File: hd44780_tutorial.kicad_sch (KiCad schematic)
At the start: 28 parts, among them J1 LCD_2004_PinSocket_1x16_P2.54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, J2 USB4105-GF-A, SW1 REG SELECT, SW2 ENABLE, SW3 DS02C-254-1L-08BE

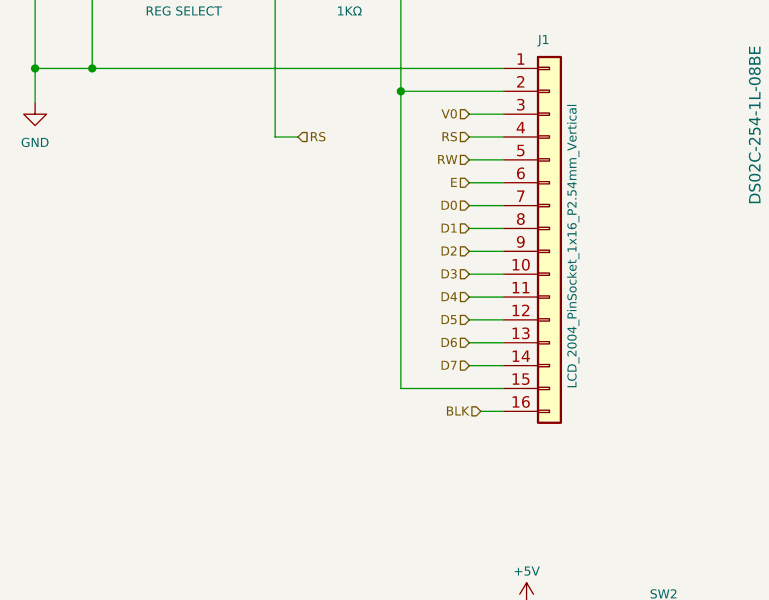
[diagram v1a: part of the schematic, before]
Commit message: Adjusted some copper tracks. Made all resistors horizontal. Added 1K network resistor for LCD data lines. Updated version number to 1.0a and date to 3/15/2024.
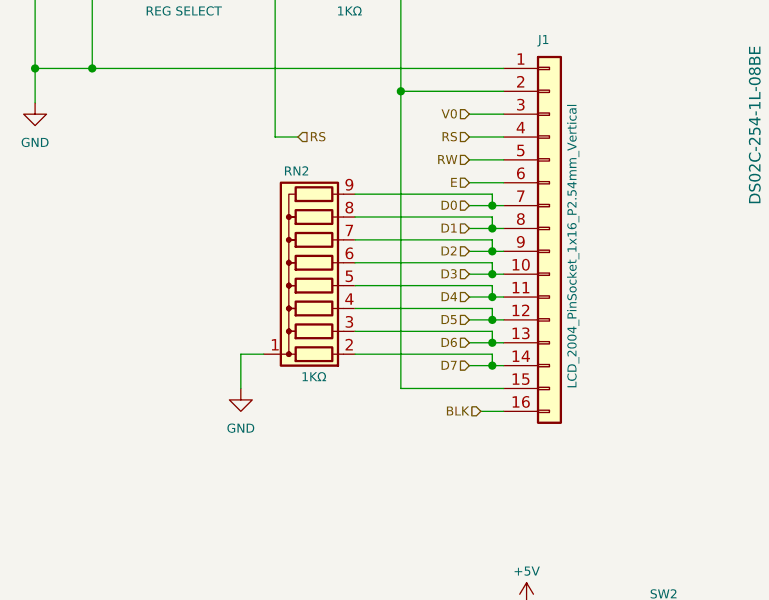
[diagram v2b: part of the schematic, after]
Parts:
- added RN2: 1KΩ, footprints:R_Array_SIP9, symbol hd44780_tutorial:R_Network08
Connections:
- net D0: now also RN2.9 (R8)
- net D1: now also RN2.8 (R7)
- net D2: now also RN2.7 (R6)
- net D3: now also RN2.6 (R5)
- net D4: now also RN2.5 (R4)
- net D5: now also RN2.4 (R3)
- net D6: now also RN2.3 (R2)
- net D7: now also RN2.2 (R1)
- net GND: now also RN2.1 (common)
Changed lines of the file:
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@@
   (title_block
     (title "${project_name}")
-    (date "2024-03-05")
+    (date "2024-03-15")
     (rev "${version}")
   )
@@
   (junction (at 210.82 116.84) (diameter 0) (color 0 0 0 0)
   )
+  (junction (at 68.58 110.49) (diameter 0) (color 0 0 0 0)
+  )
+  (junction (at 68.58 115.57) (diameter 0) (color 0 0 0 0)
+  )
   (junction (at 123.19 120.65) (diameter 0) (color 0 0 0 0)
   )
@@
   (junction (at 219.71 129.54) (diameter 0) (color 0 0 0 0)
   )
+  (junction (at 68.58 120.65) (diameter 0) (color 0 0 0 0)
+  )
   (junction (at 107.95 120.65) (diameter 0) (color 0 0 0 0)
   )
@@
   (junction (at 128.27 120.65) (diameter 0) (color 0 0 0 0)
   )
+  (junction (at 68.58 123.19) (diameter 0) (color 0 0 0 0)
+  )
   (junction (at 204.47 93.98) (diameter 0) (color 0 0 0 0)
   )
   (junction (at 146.05 123.19) (diameter 0) (color 0 0 0 0)
   )
+  (junction (at 68.58 113.03) (diameter 0) (color 0 0 0 0)
+  )
+  (junction (at 68.58 118.11) (diameter 0) (color 0 0 0 0)
+  )
+  (junction (at 68.58 107.95) (diameter 0) (color 0 0 0 0)
+  )
   (junction (at 149.86 130.81) (diameter 0) (color 0 0 0 0)
   )
@@
   )
   (junction (at 199.39 113.03) (diameter 0) (color 0 0 0 0)
+  )
+  (junction (at 68.58 125.73) (diameter 0) (color 0 0 0 0)
   )
   (junction (at 44.45 83.82) (diameter 0) (color 0 0 0 0)
@@
     (stroke (width 0) (type default))
   )
+  (wire (pts (xy 53.34 114.3) (xy 68.58 114.3))
+    (stroke (width 0) (type default))
+  )
   (wire (pts (xy 199.39 118.11) (xy 199.39 113.03))
     (stroke (width 0) (type default))
@@
     (stroke (width 0) (type default))
   )
+  (wire (pts (xy 68.58 111.76) (xy 68.58 113.03))
+    (stroke (width 0) (type default))
+  )
   (wire (pts (xy 66.04 102.87) (xy 69.85 102.87))
     (stroke (width 0) (type default))
   )
+  (wire (pts (xy 68.58 119.38) (xy 68.58 120.65))
+    (stroke (width 0) (type default))
+  )
   (wire (pts (xy 118.11 109.22) (xy 118.11 120.65))
     (stroke (width 0) (type default))
@@
     (stroke (width 0) (type default))
   )
-  (wire (pts (xy 66.04 110.49) (xy 69.85 110.49))
-    (stroke (width 0) (type default))
-  )
-  (wire (pts (xy 66.04 115.57) (xy 69.85 115.57))
+  (wire (pts (xy 66.04 110.49) (xy 68.58 110.49))
+    (stroke (width 0) (type default))
+  )
+  (wire (pts (xy 53.34 109.22) (xy 68.58 109.22))
+    (stroke (width 0) (type default))
+  )
+  (wire (pts (xy 66.04 115.57) (xy 68.58 115.57))
     (stroke (width 0) (type default))
   )
@@
     (stroke (width 0) (type default))
   )
+  (wire (pts (xy 68.58 109.22) (xy 68.58 110.49))
+    (stroke (width 0) (type default))
+  )
   (wire (pts (xy 111.76 46.99) (xy 105.41 46.99))
     (stroke (width 0) (type default))
   )
+  (wire (pts (xy 68.58 124.46) (xy 68.58 125.73))
+    (stroke (width 0) (type default))
+  )
   (wire (pts (xy 119.38 86.36) (xy 119.38 76.2))
     (stroke (width 0) (type default))
@@
     (stroke (width 0) (type default))
   )
+  (wire (pts (xy 68.58 110.49) (xy 69.85 110.49))
+    (stroke (width 0) (type default))
+  )
   (wire (pts (xy 118.11 120.65) (xy 123.19 120.65))
     (stroke (width 0) (type default))
@@
     (stroke (width 0) (type default))
   )
+  (wire (pts (xy 68.58 115.57) (xy 69.85 115.57))
+    (stroke (width 0) (type default))
+  )
   (wire (pts (xy 199.39 93.98) (xy 204.47 93.98))
     (stroke (width 0) (type default))
@@
     (stroke (width 0) (type default))
   )
-  (wire (pts (xy 66.04 125.73) (xy 69.85 125.73))
+  (wire (pts (xy 66.04 125.73) (xy 68.58 125.73))
     (stroke (width 0) (type default))
   )
@@
     (stroke (width 0) (type default))
   )
+  (wire (pts (xy 53.34 124.46) (xy 68.58 124.46))
+    (stroke (width 0) (type default))
+  )
+  (wire (pts (xy 53.34 111.76) (xy 68.58 111.76))
+    (stroke (width 0) (type default))
+  )
   (wire (pts (xy 118.11 86.36) (xy 118.11 93.98))
     (stroke (width 0) (type default))
@@
     (stroke (width 0) (type default))
   )
-  (wire (pts (xy 66.04 113.03) (xy 69.85 113.03))
+  (wire (pts (xy 66.04 113.03) (xy 68.58 113.03))
     (stroke (width 0) (type default))
   )
@@
     (stroke (width 0) (type default))
   )
+  (wire (pts (xy 68.58 121.92) (xy 68.58 123.19))
+    (stroke (width 0) (type default))
+  )
   (wire (pts (xy 57.15 83.82) (xy 58.42 83.82))
     (stroke (width 0) (type default))
@@
     (stroke (width 0) (type default))
   )
-  (wire (pts (xy 66.04 120.65) (xy 69.85 120.65))
+  (wire (pts (xy 66.04 120.65) (xy 68.58 120.65))
     (stroke (width 0) (type default))
   )
@@
     (stroke (width 0) (type default))
   )
+  (wire (pts (xy 68.58 118.11) (xy 69.85 118.11))
+    (stroke (width 0) (type default))
+  )
+  (wire (pts (xy 68.58 107.95) (xy 69.85 107.95))
+    (stroke (width 0) (type default))
+  )
   (wire (pts (xy 119.38 58.42) (xy 119.38 60.96))
     (stroke (width 0) (type default))
@@
     (stroke (width 0) (type default))
   )
+  (wire (pts (xy 53.34 106.68) (xy 68.58 106.68))
+    (stroke (width 0) (type default))
+  )
   (wire (pts (xy 67.31 130.81) (xy 69.85 130.81))
     (stroke (width 0) (type default))
@@
     (stroke (width 0) (type default))
   )
+  (wire (pts (xy 68.58 120.65) (xy 69.85 120.65))
+    (stroke (width 0) (type default))
+  )
   (wire (pts (xy 133.35 109.22) (xy 133.35 120.65))
     (stroke (width 0) (type default))
   )
+  (wire (pts (xy 68.58 116.84) (xy 68.58 118.11))
+    (stroke (width 0) (type default))
+  )
   (wire (pts (xy 204.47 93.98) (xy 204.47 96.52))
     (stroke (width 0) (type default))
@@
     (stroke (width 0) (type default))
   )
+  (wire (pts (xy 53.34 121.92) (xy 68.58 121.92))
+    (stroke (width 0) (type default))
+  )
   (wire (pts (xy 121.92 58.42) (xy 121.92 60.96))
     (stroke (width 0) (type default))
@@
     (stroke (width 0) (type default))
   )
+  (wire (pts (xy 40.64 124.46) (xy 40.64 128.27))
+    (stroke (width 0) (type default))
+  )
   (wire (pts (xy 107.95 83.82) (xy 114.3 83.82))
     (stroke (width 0) (type default))
@@
     (stroke (width 0) (type default))
   )
+  (wire (pts (xy 68.58 125.73) (xy 69.85 125.73))
+    (stroke (width 0) (type default))
+  )
   (wire (pts (xy 58.42 128.27) (xy 58.42 95.25))
     (stroke (width 0) (type default))
@@
     (stroke (width 0) (type default))
   )
+  (wire (pts (xy 53.34 116.84) (xy 68.58 116.84))
+    (stroke (width 0) (type default))
+  )
   (wire (pts (xy 114.3 175.26) (xy 118.11 175.26))
     (stroke (width 0) (type default))
@@
     (stroke (width 0) (type default))
   )
+  (wire (pts (xy 68.58 106.68) (xy 68.58 107.95))
+    (stroke (width 0) (type default))
+  )
   (wire (pts (xy 123.19 86.36) (xy 123.19 93.98))
     (stroke (width 0) (type default))
@@
     (stroke (width 0) (type default))
   )
+  (wire (pts (xy 68.58 114.3) (xy 68.58 115.57))
+    (stroke (width 0) (type default))
+  )
   (wire (pts (xy 123.19 154.94) (xy 118.11 154.94))
     (stroke (width 0) (type default))
   )
-  (wire (pts (xy 66.04 118.11) (xy 69.85 118.11))
+  (wire (pts (xy 53.34 119.38) (xy 68.58 119.38))
+    (stroke (width 0) (type default))
+  )
+  (wire (pts (xy 66.04 118.11) (xy 68.58 118.11))
     (stroke (width 0) (type default))
   )
@@
     (stroke (width 0) (type default))
   )
+  (wire (pts (xy 68.58 113.03) (xy 69.85 113.03))
+    (stroke (width 0) (type default))
+  )
   (wire (pts (xy 118.11 175.26) (xy 118.11 181.61))
     (stroke (width 0) (type default))
   )
-  (wire (pts (xy 66.04 123.19) (xy 69.85 123.19))
+  (wire (pts (xy 66.04 123.19) (xy 68.58 123.19))
     (stroke (width 0) (type default))
   )
@@
     (stroke (width 0) (type default))
   )
-  (wire (pts (xy 66.04 107.95) (xy 69.85 107.95))
+  (wire (pts (xy 66.04 107.95) (xy 68.58 107.95))
     (stroke (width 0) (type default))
   )
@@
     (stroke (width 0) (type default))
   )
+  (wire (pts (xy 43.18 124.46) (xy 40.64 124.46))
+    (stroke (width 0) (type default))
+  )
   (wire (pts (xy 102.87 128.27) (xy 106.68 128.27))
     (stroke (width 0) (type default))
@@
   )
   (wire (pts (xy 128.27 109.22) (xy 128.27 120.65))
+    (stroke (width 0) (type default))
+  )
+  (wire (pts (xy 68.58 123.19) (xy 69.85 123.19))
     (stroke (width 0) (type default))
   )
@@
         (path "/5361679f-cf45-4efb-b33e-2203c0026607"
           (reference "RV2") (unit 1)
+        )
+      )
+    )
+  )
+  (symbol (lib_id "power:GND") (at 40.64 128.27 0) (unit 1)
+    (in_bom yes) (on_board yes) (dnp no) (fields_autoplaced)
+    (property "Reference" "#PWR08" (at 40.64 134.62 0)
+      (effects (font (size 1 1)) hide)
+    )
+    (property "Value" "GND" (at 40.64 132.715 0)
+      (effects (font (size 1 1)))
+    )
+    (property "Footprint" "" (at 40.64 128.27 0)
+      (effects (font (size 1 1)) hide)
+    )
+    (property "Datasheet" "" (at 40.64 128.27 0)
+      (effects (font (size 1 1)) hide)
+    )
+    (pin "1")
+    (instances
+      (project "hd44780_tutorial"
+        (path "/5361679f-cf45-4efb-b33e-2203c0026607"
+          (reference "#PWR08") (unit 1)
         )
       )
@@
         )
       )
+    )
+  )
+  (symbol (lib_id "hd44780_tutorial:R_Network08") (at 48.26 114.3 90) (unit 1)
+    (in_bom yes) (on_board yes) (dnp no)
+    (property "Reference" "RN2" (at 48.26 104.14 90)
+      (effects (font (size 1 1)) (justify left))
+    )
+    (property "Value" "1KΩ" (at 50.165 127 90)
+      (effects (font (size 1 1)) (justify left))
+    )
+    (property "Footprint" "footprints:R_Array_SIP9" (at 48.26 102.235 90)
+      (effects (font (size 1 1)) hide)
+    )
+    (property "Datasheet" "http://www.vishay.com/docs/31509/csc.pdf" (at 48.26 114.3 0)
+      (effects (font (size 1 1)) hide)
+    )
+    (pin "9")
+    (pin "2")
+    (pin "1")
+    (pin "3")
+    (pin "5")
+    (pin "6")
+    (pin "7")
+    (pin "4")
+    (pin "8")
+    (instances
+      (project "hd44780_tutorial"
+        (path "/5361679f-cf45-4efb-b33e-2203c0026607"
+          (reference "RN2") (unit 1)
+        )
+      )
